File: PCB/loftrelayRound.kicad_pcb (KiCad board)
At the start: 2 copper layers, 70.1 x 70.1 mm, 29 parts, among them J1 PowerIn, J2 Load, J3 SenSor, J4 Program, K1 G5Q-14-EU DC5, Q1 2N7002, U1 AP1117-33, U2 PC817, U4 ESP-12E

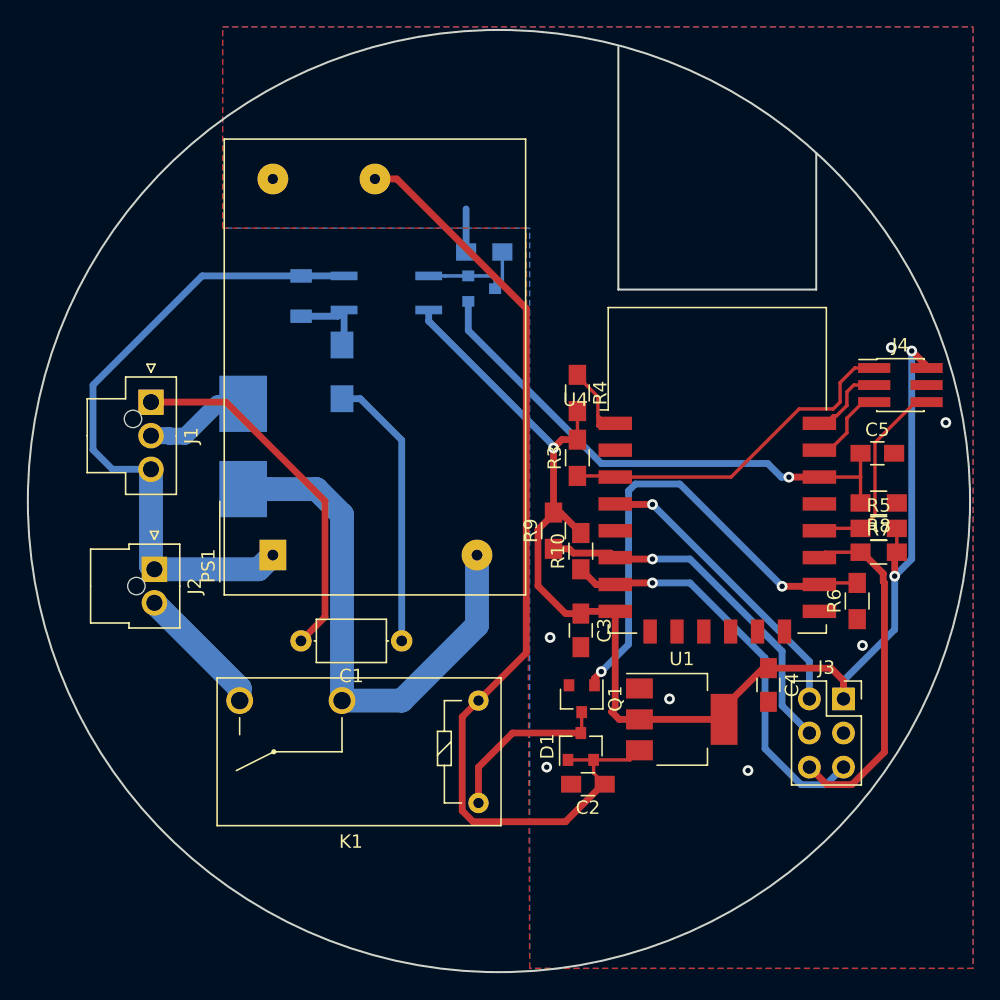
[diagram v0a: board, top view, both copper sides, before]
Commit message: change in sensor, made for HA
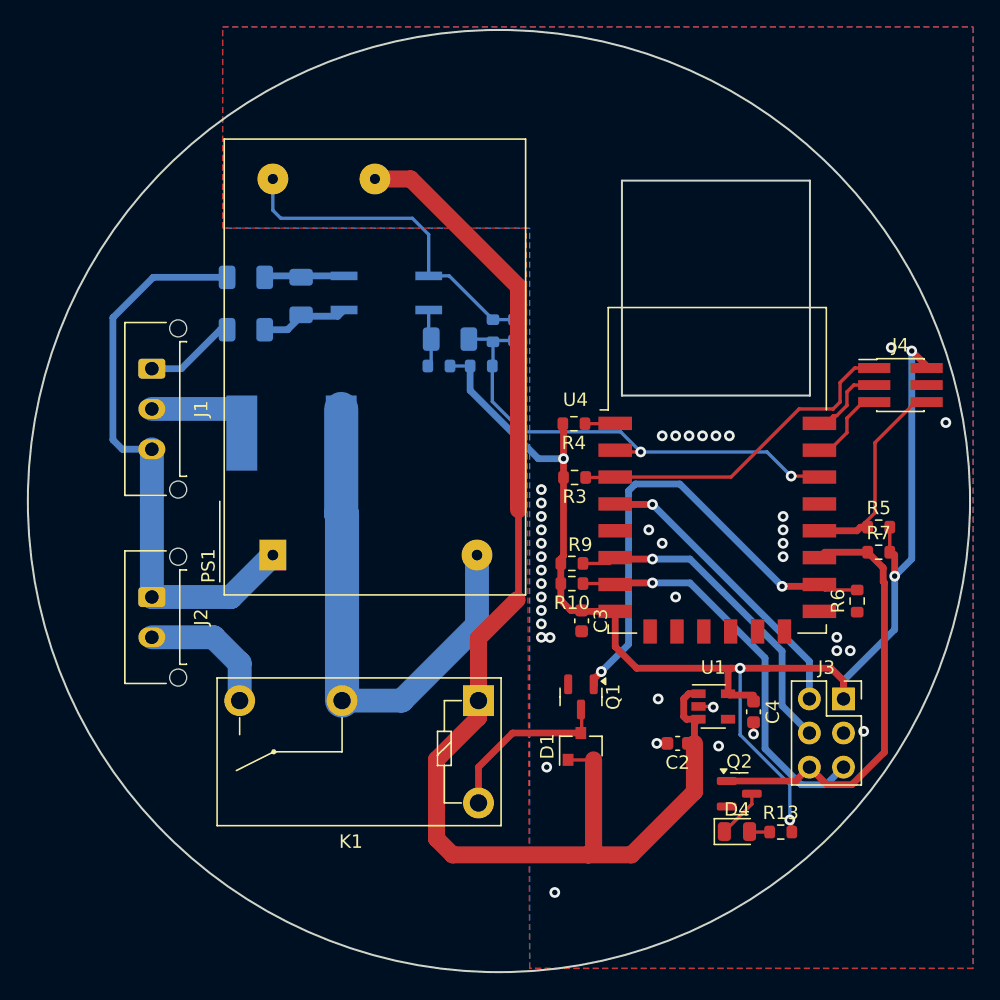
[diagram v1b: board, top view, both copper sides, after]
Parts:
- removed C1: 33nF, Capacitors_THT:C_Axial_L5.1mm_D3.1mm_P7.50mm_Horizontal
- added D4: LED, LED_SMD:LED_0805_2012Metric, F.Cu at (166.6, 142.5)
- added Q2: Sq2318AES, Package_TO_SOT_SMD:SOT-23, F.Cu at (166.7, 139.7)
- added R11: 100k, Resistor_SMD:R_0603_1608Metric, B.Cu at (144.4, 107.8)
- added R12: 100k, Resistor_SMD:R_0603_1608Metric, B.Cu at (147.5, 107.8)
- added R13: 100, Resistor_SMD:R_0603_1608Metric, F.Cu at (169.8, 142.5)
- C2, C3, C4: value 22uF -> 1uF; footprint Capacitors_SMD:C_0805_HandSoldering -> Capacitor_SMD:C_0603_1608Metric
- C5: value 100nF -> 2u2; footprint Capacitors_SMD:C_0805_HandSoldering -> Capacitor_SMD:C_0603_1608Metric; moved to B.Cu
- D2: footprint Diodes_SMD:D_1206 -> Diode_SMD:D_1206_3216Metric
- D3: value BAT54A -> D; footprint Package_TO_SOT_SMD:SOT-23 -> Diode_SMD:D_1206_3216Metric
- F1: footprint SMD_Packages:Fuse_SMD -> GL_Diverse:Fuse_SMD2920
- J1: footprint Connectors_Molex:Molex_NanoFit_1x03x2.50mm_Straight -> Connector_Molex:Molex_Micro-Fit_3.0_43650-0315_1x03_P3.00mm_Vertical
- J2: footprint Connectors_Molex:Molex_NanoFit_1x02x2.50mm_Straight -> Connector_Molex:Molex_Micro-Fit_3.0_43650-0215_1x02_P3.00mm_Vertical
- K1: footprint Relays_THT:Relay_SPST_OMRON-G5Q -> Relay_THT:Relay_SPST_Omron-G5Q-1A
- Q1: value 2N7002 -> Sq2318AES; footprint TO_SOT_Packages_SMD:SOT-23 -> Package_TO_SOT_SMD:SOT-23
- R1: value 100R -> 100k; footprint Resistors_SMD:R_1206_HandSoldering -> Resistor_SMD:R_1206_3216Metric
- R10, R3, R4, R5, R6, R7, R9: footprint Resistors_SMD:R_0805_HandSoldering -> Resistor_SMD:R_0603_1608Metric
- R2: value 100k -> 1M; footprint Resistors_SMD:R_0805_HandSoldering -> Resistor_SMD:R_0603_1608Metric
- R8: value 10k -> 100k; footprint Resistors_SMD:R_0805_HandSoldering -> Resistor_SMD:R_1206_3216Metric; moved to B.Cu
- U1: value AP1117-33 -> AP2112K-3.3; footprint Package_TO_SOT_SMD:SOT-223-3_TabPin2 -> Package_TO_SOT_SMD:SOT-23-5
- U2: value PC817 -> LTV-355T
- moved R8 50.0 mm to (130.0, 101.2)
- moved C5 28.5 mm to (150.0, 105.1), turned to 90 degrees
- moved R1 7.82 mm to (130.0, 105.1), turned to 180 degrees
- moved C2 7.34 mm to (162.2, 135.9)
- moved R2 5.90 mm to (148.4, 105.2), turned to -90 degrees
- moved D3 4.44 mm to (145.2, 105.8)
- moved F1 3.74 mm to (133.4, 112.8), turned to 180 degrees
- moved R9 2.80 mm to (154.3, 122.5), turned to 180 degrees
- moved U1 2.53 mm to (164.8, 133.2)
- moved R10 2.50 mm to (154.3, 124.0), turned to 180 degrees
- moved J1 2.49 mm to (123.0, 108.0)
- moved R4 2.31 mm to (154.4, 112.1), turned to 180 degrees
- moved C4 2.29 mm to (167.8, 133.6)
- moved J2 2.07 mm to (123.0, 125.0)
- moved R3 1.48 mm to (154.5, 116.1), turned to 180 degrees
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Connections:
- net /D0 renamed /ESP8266/D0
- net /EN renamed /ESP8266/EN
- net /RX renamed /ESP8266/RX
- net /TX renamed /ESP8266/TX
- net Net-(J3-Pad2) renamed /ESP8266/D16
- net Net-(J3-Pad4) renamed /ESP8266/D12
- net Net-(J3-Pad5) renamed /ESP8266/D13
- net Net-(J3-Pad6) renamed /ESP8266/D2
- net Net-(Q1-Pad1) renamed /ESP8266/D15
- C2 pad 2: GNDD -> GND
- C3 pad 2: GNDD -> GND
- C4 pad 2: GNDD -> GND
- C5 pad 2: GNDD -> GND
- D2 pad 2: Net-(D2-Pad2) -> Net-(D2-A)
- D3 pad 1: /Opto -> Net-(D3-K)
- D3 pad 2: Net-(D3-Pad2) -> /Opto
- J1 pad 1: Net-(C1-Pad2) -> Net-(J1-Pin_1)
- J1 pad 3: Net-(D2-Pad2) -> Net-(J1-Pin_3)
- J2 pad 1: Net-(D2-Pad2) -> Net-(J1-Pin_3)
- J3 pad 3: GNDD -> GND
- J4 pad 4: GNDD -> GND
- PS1 pad 1: Net-(D2-Pad2) -> Net-(J1-Pin_3)
- PS1 pad 3: GNDD -> GND
- Q1 pad 2: GNDD -> GND
- R1 pad 2: Net-(C1-Pad1) -> Net-(J1-Pin_1)
- R2 pad 1: GNDD -> GND
- R2 pad 2: Net-(D3-Pad2) -> /Opto
- R6 pad 1: GNDD -> GND
- R8 pad 1: GNDD -> Net-(D2-A)
- R8 pad 2: /Opto -> Net-(J1-Pin_3)
- U1 pad 1: GNDD -> +5V
- U1 pad 2: +3V3 -> GND
- U2 pad 2: Net-(D2-Pad2) -> Net-(D2-A)
- U2 pad 3: Net-(D3-Pad2) -> GND
- U2 pad 4: +3V3 -> Net-(D3-K)
- U4 pad 10: (no net) -> unconnected-(U4-MISO-Pad10)
- U4 pad 11: (no net) -> unconnected-(U4-GPIO9-Pad11)
- U4 pad 12: (no net) -> unconnected-(U4-GPIO10-Pad12)
- U4 pad 13: (no net) -> unconnected-(U4-MOSI-Pad13)
- U4 pad 14: (no net) -> unconnected-(U4-SCLK-Pad14)
- U4 pad 15: GNDD -> GND
- U4 pad 19: (no net) -> /ESP8266/D4
- U4 pad 2: (no net) -> /Opto
- U4 pad 5: (no net) -> /ESP8266/D14
- U4 pad 9: (no net) -> unconnected-(U4-CS0-Pad9)
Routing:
- net Net-(D2-Pad2): track 48.6 -> 0.00 mm
- net Net-(J1-Pin_3): track 0.00 -> 43.3 mm
- net GND: track 0.00 -> 28.3 mm, vias 0 -> 39
- net Net-(C1-Pad2): track 27.2 -> 0.00 mm
- net +5V: track 75.1 -> 98.3 mm
- net Net-(C1-Pad1): track 20.7 -> 0.00 mm
- net Net-(D3-Pad2): track 8.67 -> 0.00 mm
- net /ESP8266/D2: track 26.0 -> 32.9 mm
- net Net-(J1-Pin_1): track 0.00 -> 6.80 mm
- net Net-(D2-A): track 0.00 -> 5.96 mm
- net Net-(U4-~{RST}): track 7.34 -> 2.26 mm
- net Net-(D3-K): track 0.00 -> 4.35 mm
- net Net-(D4-K): track 0.00 -> 3.66 mm
- net /Opto: track 40.2 -> 36.6 mm, vias 1 -> 2
- net GNDD: track 3.21 -> 0.00 mm, vias 7 -> 0
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- added copper zone on B.Cu, net GND
- added copper zone on F.Cu, net GND
- removed copper zone on B.Cu, net GNDD
- removed copper zone on F.Cu, net GNDD
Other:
- outline, holes or cut-outs redrawn
- net class Default removed
